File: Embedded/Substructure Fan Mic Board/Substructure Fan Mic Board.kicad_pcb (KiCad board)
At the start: 2 copper layers, 11 parts, among them J1 Conn_01x03_Socket, J2 Conn_01x02_Socket, J3 Conn_01x02_Socket, Q1 DMG3402L, Q2 DMG3402L, U2 F FFC

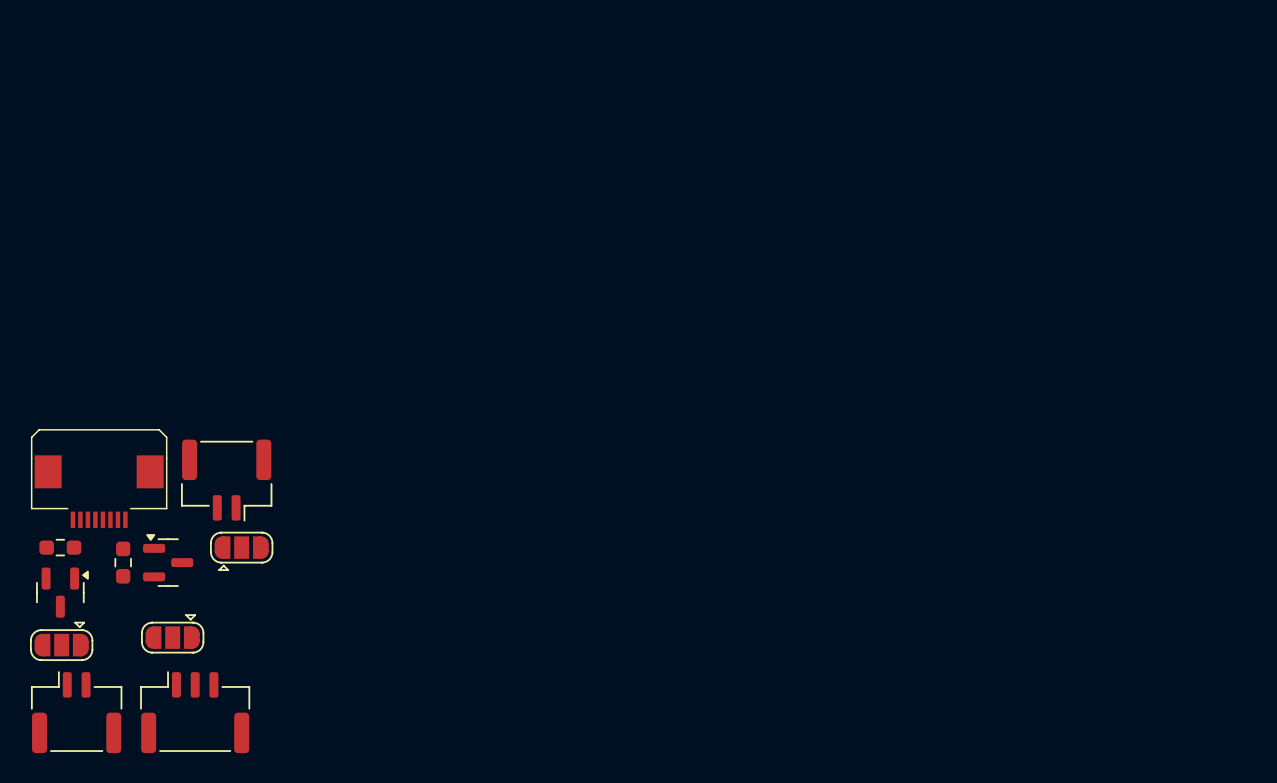
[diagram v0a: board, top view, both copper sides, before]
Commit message: Added Component Placement Optimisation & Board Edge & Routing
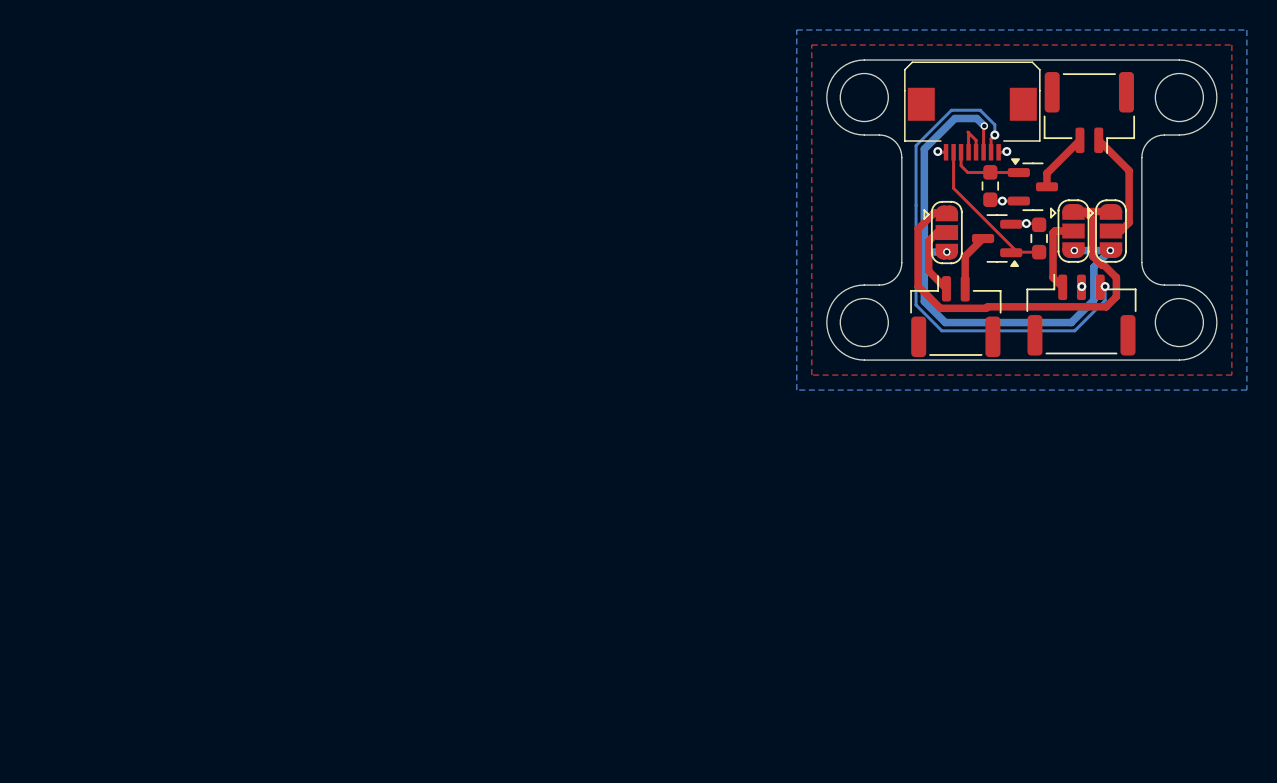
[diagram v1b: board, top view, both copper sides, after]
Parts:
- moved R2 68.4 mm to (99.2, 71.9), turned to 90 degrees
- moved Q2 66.8 mm to (96.4, 71.9), turned to 180 degrees
- moved JP1 65.9 mm to (101.4, 71.4), turned to -90 degrees
- moved JP3 65.1 mm to (93.0, 71.5), turned to -90 degrees
- moved J1 64.7 mm to (102.0, 77.0)
- moved J3 64.3 mm to (93.6, 77.1)
- moved U2 63.1 mm to (94.7, 65.5)
- moved R1 63.0 mm to (95.9, 68.4)
- moved Q1 62.8 mm to (98.7, 68.5)
- moved J2 62.5 mm to (102.5, 63.5)
- moved JP2 61.7 mm to (103.9, 71.4), turned to -90 degrees
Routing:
- net +3V3: track 0.00 -> 37.2 mm, vias 0 -> 4
- net Mic Analog: track 0.00 -> 34.6 mm, vias 0 -> 2
- net +5V: track 0.00 -> 33.1 mm
- net Fan 1: track 0.00 -> 9.87 mm
- net Net-(J2-Pin_1): track 0.00 -> 7.77 mm
- net Net-(J1-Pin_1): track 0.00 -> 5.31 mm
- net Net-(J3-Pin_1): track 0.00 -> 5.12 mm
- net Fan 0: track 0.00 -> 4.94 mm
- net GND: track 0.00 -> 4.92 mm, vias 0 -> 5
- net Net-(J2-Pin_2): track 0.00 -> 4.01 mm
- net Net-(J3-Pin_2): track 0.00 -> 3.85 mm
- added copper zone on F.Cu, net +5V
- added copper zone on B.Cu, net GND
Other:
- board outline added: 26 x 20 mm

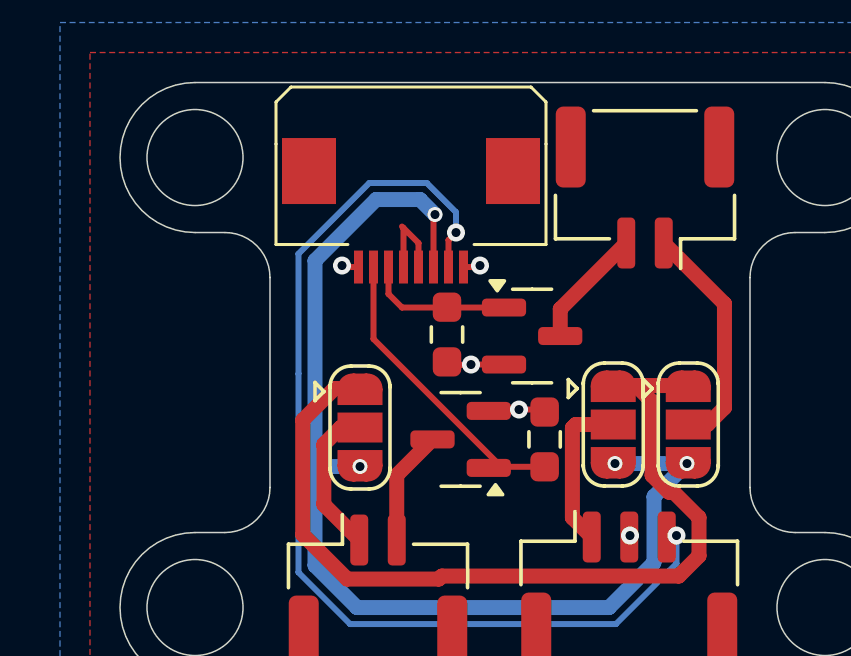
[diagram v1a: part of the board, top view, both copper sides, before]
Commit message: Modified Ports to fit FFC orientations
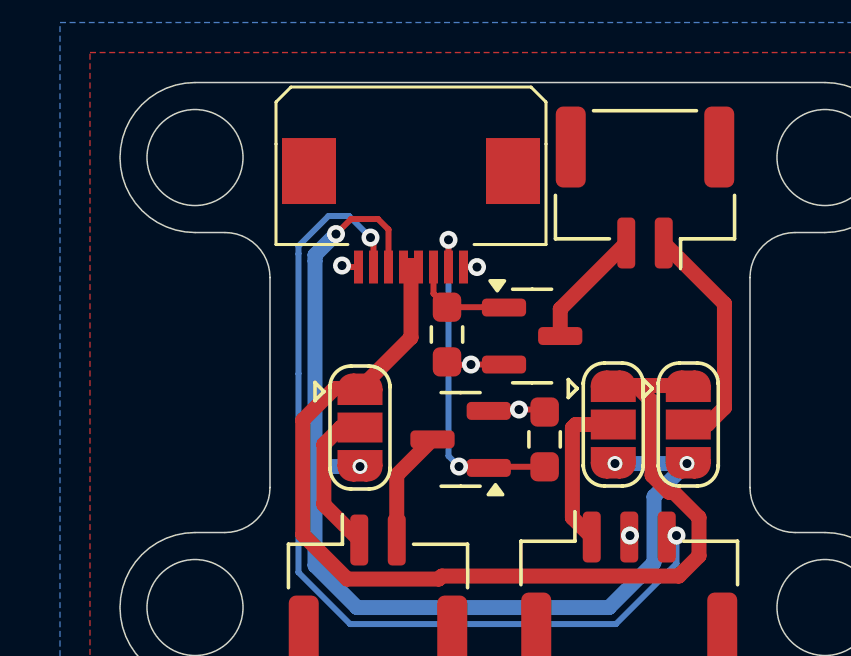
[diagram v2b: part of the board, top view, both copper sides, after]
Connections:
- U2 pad 2: Mic Analog -> Fan 1
- U2 pad 3: +3V3 -> Fan 0
- U2 pad 6: Fan 0 -> +3V3
- U2 pad 7: Fan 1 -> Mic Analog
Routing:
- net Mic Analog: track 34.6 -> 30.4 mm
- net +5V: track 33.1 -> 35.4 mm
- net +3V3: track 37.2 -> 34.9 mm
- net Fan 0: track 4.94 -> 3.43 mm
- net Fan 1: track 9.87 -> 11.1 mm, vias 0 -> 2

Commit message: Added Logos
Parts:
- added G***: LOGO, LOGO, B.Cu at (98.0, 70.5)
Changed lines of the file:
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@@
 		)
+	)
+	(footprint "LOGO"
+		(layer "B.Cu")
+		(at 98 70.5 180)
+		(property "Reference" "G***"
+			(at 0 0 0)
+			(layer "B.SilkS")
+			(hide yes)
+			(effects
+				(font
+					(size 1.5 1.5)
+					(thickness 0.3)
+				)
+				(justify mirror)
+			)
+		)
+		(property "Value" "LOGO"
+			(at 0.75 0 0)
+			(layer "B.SilkS")
+			(hide yes)
+			(effects
+				(font
+					(size 1.5 1.5)
+					(thickness 0.3)
+				)
+				(justify mirror)
+			)
+		)
+		(property "Datasheet" ""
+			(at 0 0 0)
+			(layer "B.Fab")
+			(hide yes)
+			(effects
+				(font
+					(size 1.27 1.27)
+					(thickness 0.15)
+				)
+				(justify mirror)
+			)
+		)
+		(property "Description" ""
+			(at 0 0 0)
+			(layer "B.Fab")
+			(hide yes)
+			(effects
+				(font
+					(size 1.27 1.27)
+					(thickness 0.15)
+				)
+				(justify mirror)
+			)
+		)
+		(attr board_only exclude_from_pos_files exclude_from_bom)
+		(fp_poly
+			(pts
+				(xy 2.297355 1.399853) (xy 2.425981 1.233782) (xy 2.594527 0.988878) (xy 2.786639 0.691264) (xy 2.985966 0.367064)
+				(xy 3.176156 0.042399) (xy 3.340856 -0.256606) (xy 3.463716 -0.503829) (xy 3.484683 -0.551435) (xy 3.632319 -0.932866)
+				(xy 3.769731 -1.349654) (xy 3.885568 -1.76073) (xy 3.968482 -2.125024) (xy 4.007121 -2.401464) (xy 4.008554 -2.447088)
+				(xy 3.982905 -2.594393) (xy 3.896406 -2.648933) (xy 3.734726 -2.608779) (xy 3.483536 -2.472004)
+				(xy 3.296754 -2.351368) (xy 2.775785 -2.031367) (xy 2.284269 -1.783532) (xy 1.850089 -1.620751)
+				(xy 1.593489 -1.564083) (xy 1.300882 -1.505648) (xy 1.153337 -1.419241) (xy 1.146859 -1.292318)
+				(xy 1.277452 -1.112333) (xy 1.408737 -0.983902) (xy 1.785575 -0.55174) (xy 2.032278 -0.060547) (xy 2.155084 0.50461)
+				(xy 2.172078 0.842826) (xy 2.178265 1.125944) (xy 2.194061 1.340863) (xy 2.216473 1.452656) (xy 2.224999 1.460968)
+			)
+			(stroke
+				(width 0)
+				(type solid)
+			)
+			(fill yes)
+			(layer "B.SilkS")
+		)
+		(fp_poly
+			(pts
+				(xy -0.080498 2.793867) (xy 0.291311 2.759704) (xy 0.587531 2.694994) (xy 0.832749 2.593627) (xy 1.051554 2.449489)
+				(xy 1.268535 2.25647) (xy 1.351314 2.173453) (xy 1.629065 1.843441) (xy 1.802448 1.509869) (xy 1.889951 1.124665)
+				(xy 1.910619 0.719433) (xy 1.874321 0.272492) (xy 1.751872 -0.095506) (xy 1.522938 -0.440243) (xy 1.460158 -0.514064)
+				(xy 1.071066 -0.872589) (xy 0.639858 -1.096508) (xy 0.136236 -1.200339) (xy 0.01081 -1.208593) (xy -0.28665 -1.211925)
+				(xy -0.548701 -1.197744) (xy -0.716176 -1.169687) (xy -0.970994 -1.068617) (xy -1.219156 -0.925512)
+				(xy -1.503404 -0.713589) (xy -1.685842 -0.56205) (xy -2.035598 -0.28027) (xy -2.350653 -0.070026)
+				(xy -2.686801 0.100164) (xy -3.09984 0.261782) (xy -3.22183 0.304598) (xy -3.50878 0.408231) (xy -3.746001 0.502084)
+				(xy -3.893486 0.570061) (xy -3.914898 0.58349) (xy -3.991925 0.729281) (xy -3.993518 0.778936) (xy -0.785061 0.778936)
+				(xy -0.723776 0.487191) (xy -0.558521 0.268436) (xy -0.323182 0.136914) (xy -0.051644 0.106867)
+				(xy 0.222207 0.192536) (xy 0.363689 0.296128) (xy 0.528523 0.538856) (xy 0.573961 0.818218) (xy 0.507321 1.09203)
+				(xy 0.335916 1.318106) (xy 0.168648 1.420805) (xy -0.136928 1.479431) (xy -0.414389 1.408777) (xy -0.633194 1.229397)
+				(xy -0.762805 0.961845) (xy -0.785061 0.778936) (xy -3.993518 0.778936) (xy -3.999554 0.96714) (xy -3.946933 1.261518)
+				(xy -3.843211 1.576864) (xy -3.697536 1.877631) (xy -3.519057 2.128267) (xy -3.51668 2.130906) (xy -3.290422 2.331536)
+				(xy -3.00711 2.518533) (xy -2.865304 2.59051) (xy -2.706517 2.654574) (xy -2.544772 2.701979) (xy -2.352391 2.736022)
+				(xy -2.101697 2.760002) (xy -1.765009 2.777217) (xy -1.314651 2.790965) (xy -1.149238 2.795) (xy -0.552485 2.803595)
+			)
+			(stroke
+				(width 0)
+				(type solid)
+			)
+			(fill yes)
+			(layer "B.SilkS")
+		)
+		(embedded_fonts no)
 	)
 	(gr_circle
